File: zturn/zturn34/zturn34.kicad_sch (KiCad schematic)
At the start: 37 parts, among them U1 74AXP4T245, U10 74AXP4T245, U11 74AXP4T245, U12 74AXP4T245, U2 74AXP4T245, U3 74AXP4T245, U4 74AXP4T245, U5 74AXP4T245, U9 74AXP4T245

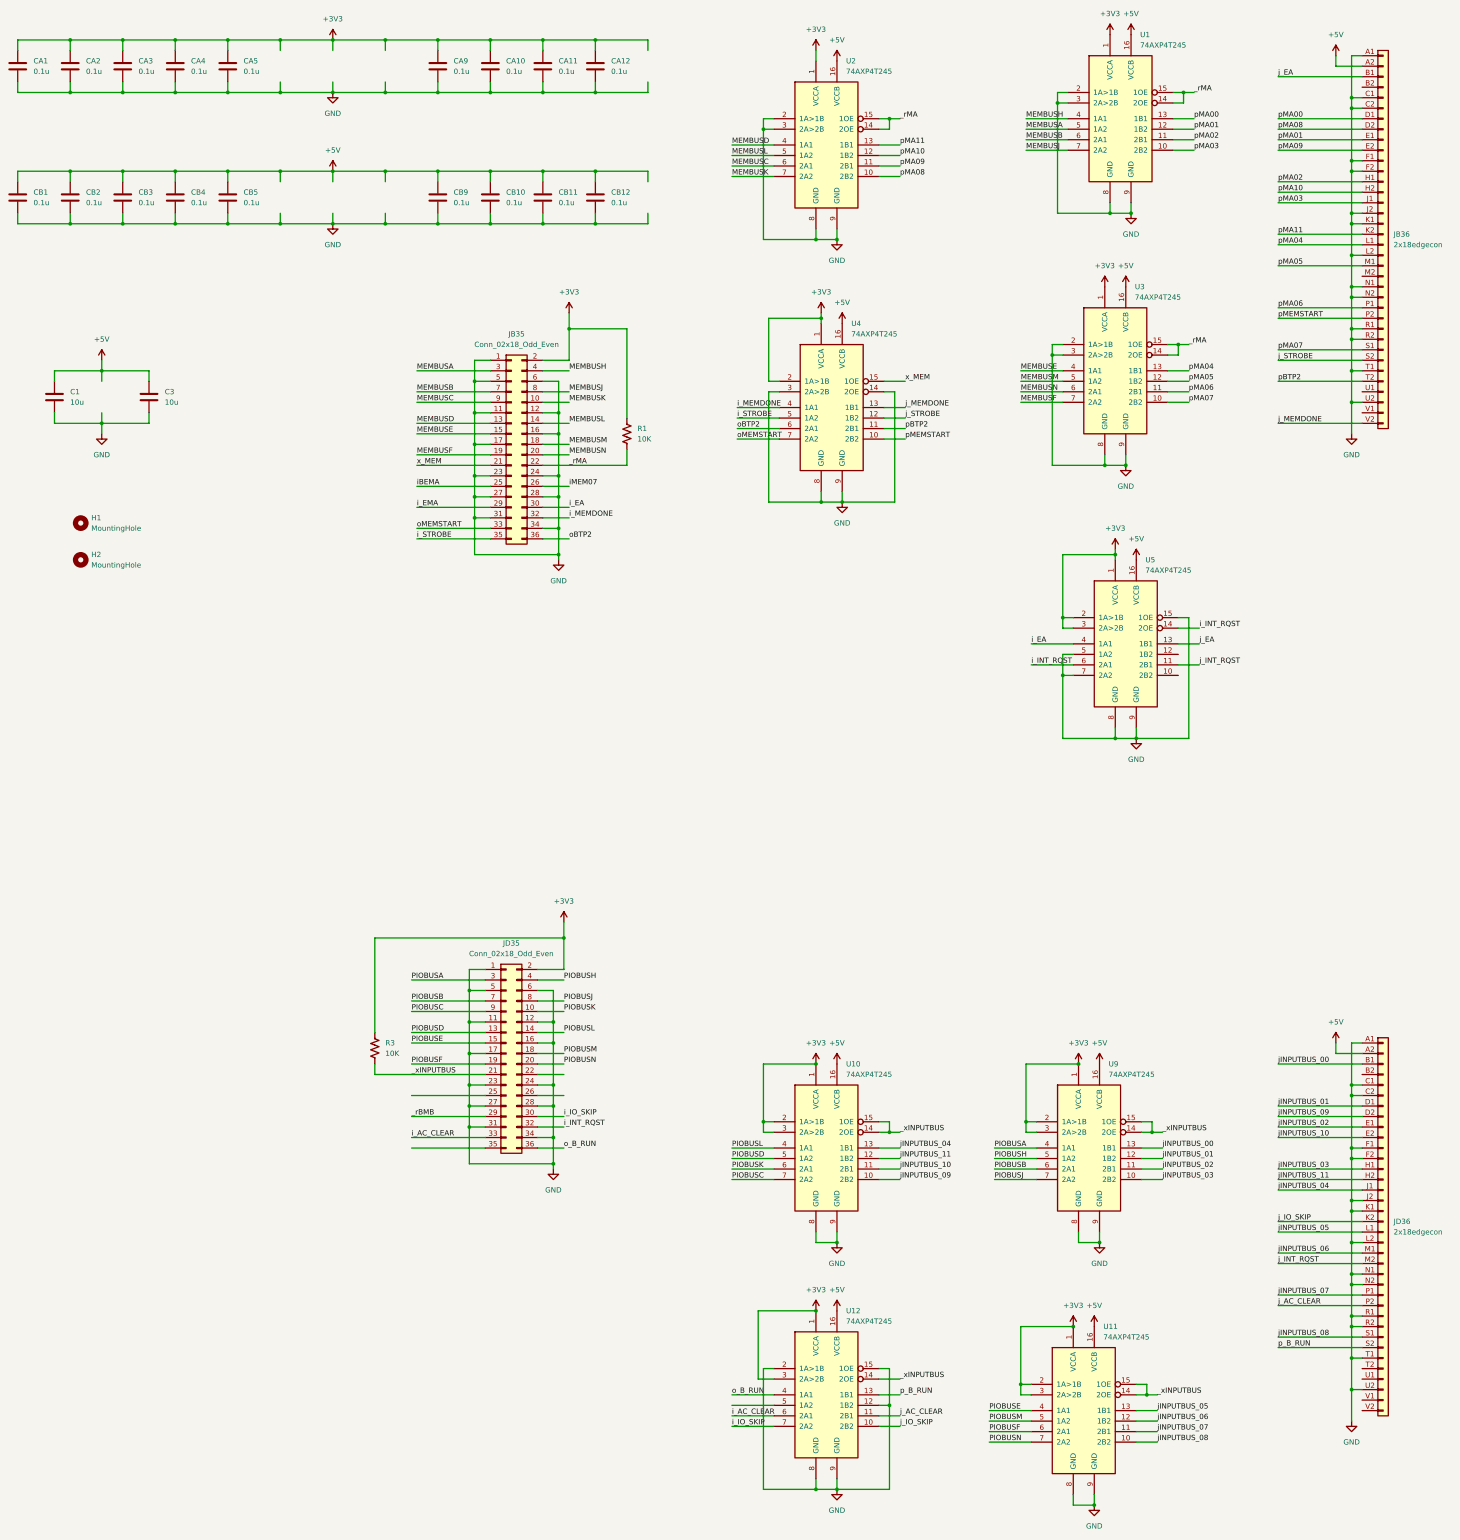
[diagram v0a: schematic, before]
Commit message: update zturn34,35 pcbs - move 10uF caps, add fiducials
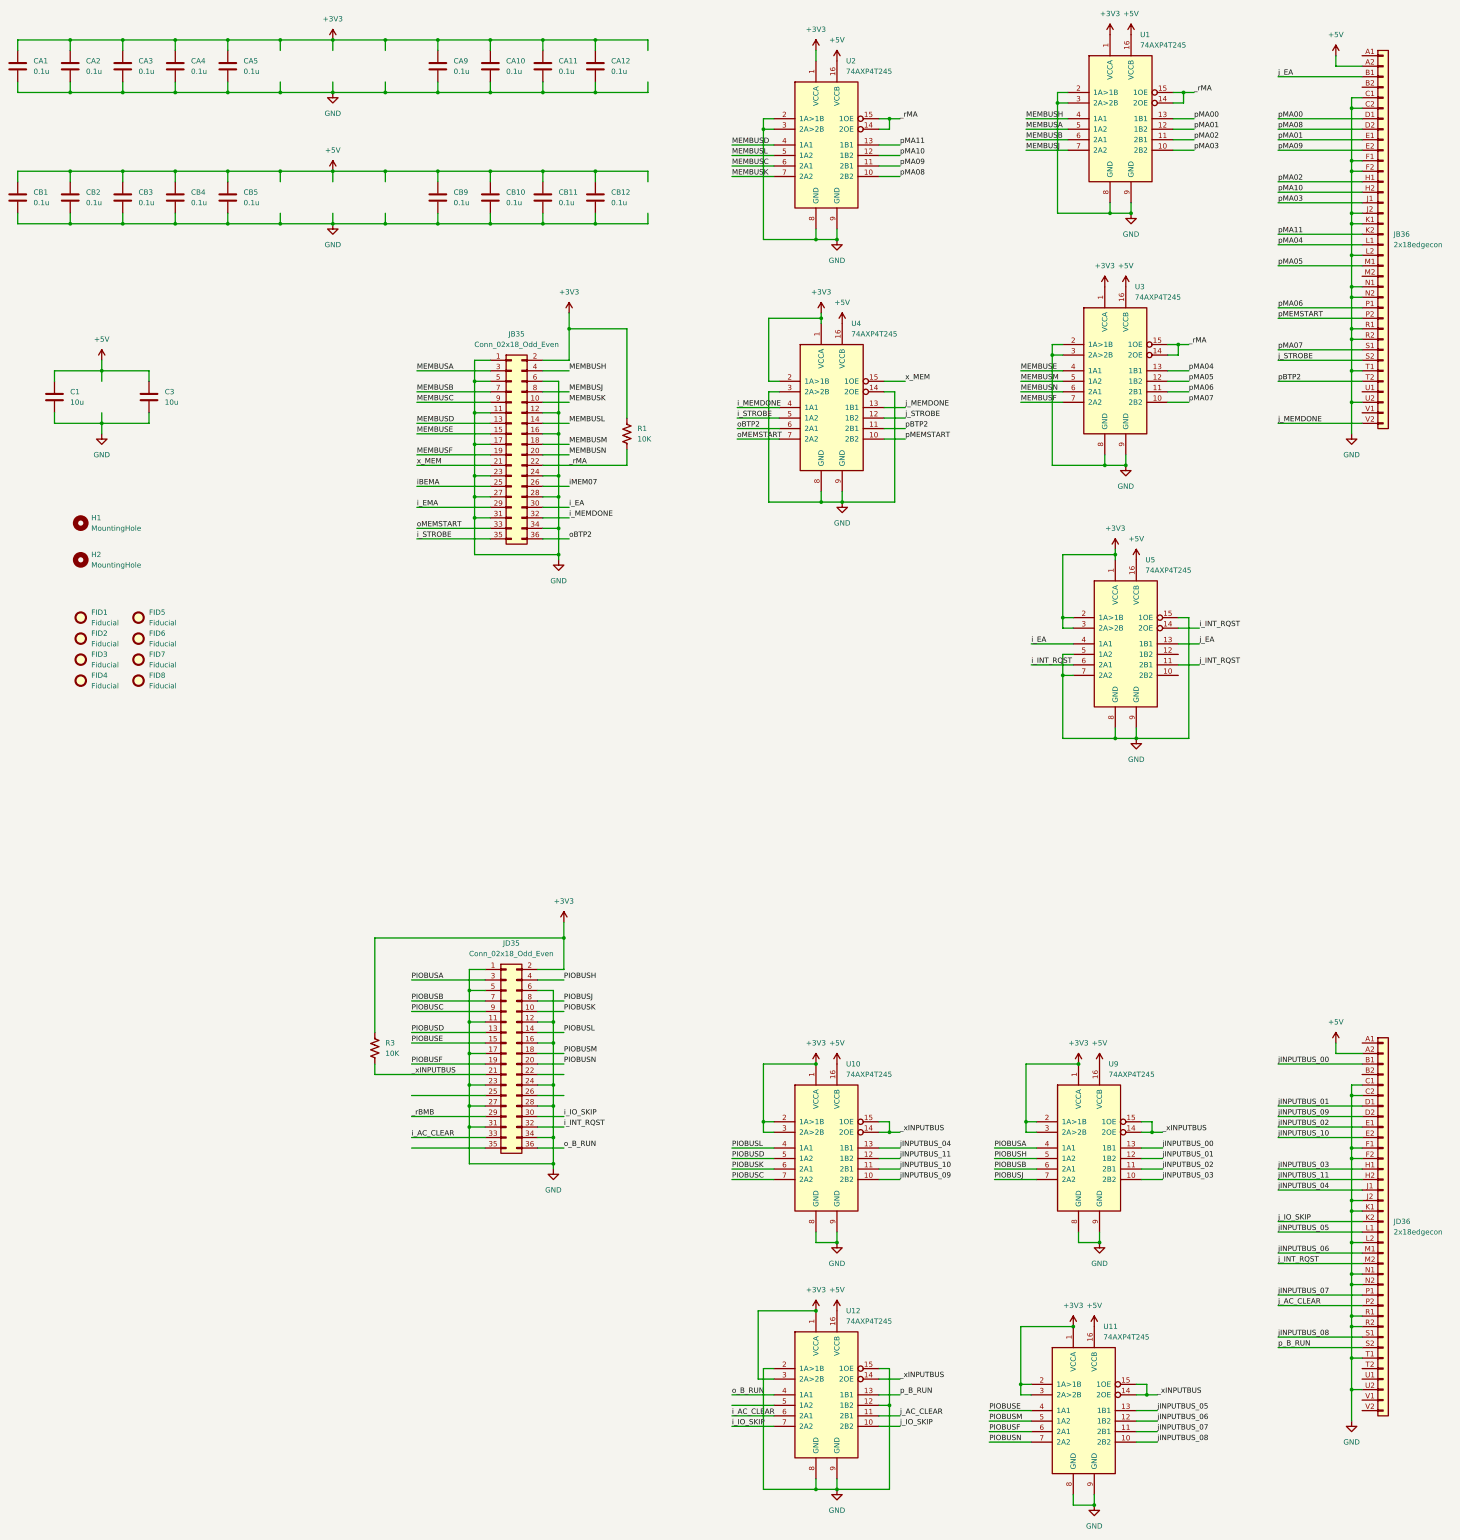
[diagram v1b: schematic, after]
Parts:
- added FID1, FID2, FID3, FID4, FID5, FID6, FID7, FID8: Fiducial, Fiducial:Fiducial_1mm_Mask2mm, symbol Mechanical:Fiducial
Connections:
- net GND: no longer JB36.A1, JD36.A1
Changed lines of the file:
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@@
   (junction (at 364.49 124.46) (diameter 0) (color 0 0 0 0)
   )
-  (junction (at 576.58 33.02) (diameter 0) (color 0 0 0 0)
-  )
   (junction (at 383.54 256.54) (diameter 0) (color 0 0 0 0)
   )
@@
   (junction (at 447.04 326.39) (diameter 0) (color 0 0 0 0)
   )
-  (junction (at 576.58 271.78) (diameter 0) (color 0 0 0 0)
-  )
   (junction (at 521.97 121.92) (diameter 0) (color 0 0 0 0)
   )
@@
     (stroke (width 0) (type default))
   )
-  (wire (pts (xy 576.58 22.86) (xy 579.12 22.86))
-    (stroke (width 0) (type default))
-  )
   (wire (pts (xy 393.7 31.75) (xy 406.4 31.75))
     (stroke (width 0) (type default))
@@
     (stroke (width 0) (type default))
   )
-  (wire (pts (xy 576.58 271.78) (xy 576.58 261.62))
-    (stroke (width 0) (type default))
-  )
   (wire (pts (xy 379.73 254) (xy 386.08 254))
     (stroke (width 0) (type default))
@@
     (stroke (width 0) (type default))
   )
-  (wire (pts (xy 576.58 261.62) (xy 579.12 261.62))
-    (stroke (width 0) (type default))
-  )
   (wire (pts (xy 532.13 99.06) (xy 537.21 99.06))
     (stroke (width 0) (type default))
@@
     (stroke (width 0) (type default))
   )
-  (wire (pts (xy 576.58 33.02) (xy 576.58 22.86))
-    (stroke (width 0) (type default))
-  )
   (wire (pts (xy 534.67 170.18) (xy 539.75 170.18))
     (stroke (width 0) (type default))
@@
     )
   )
+  (symbol (lib_id "Mechanical:Fiducial") (at 283.21 168.91 0) (unit 1)
+    (in_bom yes) (on_board yes) (dnp no) (fields_autoplaced)
+    (property "Reference" "FID7" (at 285.75 167.64 0)
+      (effects (font (size 1.27 1.27)) (justify left))
+    )
+    (property "Value" "Fiducial" (at 285.75 170.18 0)
+      (effects (font (size 1.27 1.27)) (justify left))
+    )
+    (property "Footprint" "Fiducial:Fiducial_1mm_Mask2mm" (at 283.21 168.91 0)
+      (effects (font (size 1.27 1.27)) hide)
+    )
+    (property "Datasheet" "~" (at 283.21 168.91 0)
+      (effects (font (size 1.27 1.27)) hide)
+    )
+    (instances
+      (project "zturn34"
+        (path "/f88ff33f-ea83-4481-9378-71bec9a888d0"
+          (reference "FID7") (unit 1)
+        )
+      )
+    )
+  )
   (symbol (lib_id "power:+5V") (at 572.77 261.62 0) (unit 1)
     (in_bom yes) (on_board yes) (dnp no) (fields_autoplaced)
@@
     )
   )
+  (symbol (lib_id "Mechanical:Fiducial") (at 269.24 158.75 0) (unit 1)
+    (in_bom yes) (on_board yes) (dnp no) (fields_autoplaced)
+    (property "Reference" "FID1" (at 271.78 157.48 0)
+      (effects (font (size 1.27 1.27)) (justify left))
+    )
+    (property "Value" "Fiducial" (at 271.78 160.02 0)
+      (effects (font (size 1.27 1.27)) (justify left))
+    )
+    (property "Footprint" "Fiducial:Fiducial_1mm_Mask2mm" (at 269.24 158.75 0)
+      (effects (font (size 1.27 1.27)) hide)
+    )
+    (property "Datasheet" "~" (at 269.24 158.75 0)
+      (effects (font (size 1.27 1.27)) hide)
+    )
+    (instances
+      (project "zturn34"
+        (path "/f88ff33f-ea83-4481-9378-71bec9a888d0"
+          (reference "FID1") (unit 1)
+        )
+      )
+    )
+  )
   (symbol (lib_name "GND_1") (lib_id "power:GND") (at 330.2 63.5 0) (unit 1)
     (in_bom yes) (on_board yes) (dnp no) (fields_autoplaced)
@@
     )
   )
+  (symbol (lib_id "Mechanical:Fiducial") (at 269.24 168.91 0) (unit 1)
+    (in_bom yes) (on_board yes) (dnp no) (fields_autoplaced)
+    (property "Reference" "FID3" (at 271.78 167.64 0)
+      (effects (font (size 1.27 1.27)) (justify left))
+    )
+    (property "Value" "Fiducial" (at 271.78 170.18 0)
+      (effects (font (size 1.27 1.27)) (justify left))
+    )
+    (property "Footprint" "Fiducial:Fiducial_1mm_Mask2mm" (at 269.24 168.91 0)
+      (effects (font (size 1.27 1.27)) hide)
+    )
+    (property "Datasheet" "~" (at 269.24 168.91 0)
+      (effects (font (size 1.27 1.27)) hide)
+    )
+    (instances
+      (project "zturn34"
+        (path "/f88ff33f-ea83-4481-9378-71bec9a888d0"
+          (reference "FID3") (unit 1)
+        )
+      )
+    )
+  )
   (symbol (lib_id "mylibrary:2x18edgecon") (at 584.2 304.8 0) (unit 1)
     (in_bom yes) (on_board yes) (dnp no) (fields_autoplaced)
@@
     )
   )
+  (symbol (lib_id "Mechanical:Fiducial") (at 269.24 173.99 0) (unit 1)
+    (in_bom yes) (on_board yes) (dnp no) (fields_autoplaced)
+    (property "Reference" "FID4" (at 271.78 172.72 0)
+      (effects (font (size 1.27 1.27)) (justify left))
+    )
+    (property "Value" "Fiducial" (at 271.78 175.26 0)
+      (effects (font (size 1.27 1.27)) (justify left))
+    )
+    (property "Footprint" "Fiducial:Fiducial_1mm_Mask2mm" (at 269.24 173.99 0)
+      (effects (font (size 1.27 1.27)) hide)
+    )
+    (property "Datasheet" "~" (at 269.24 173.99 0)
+      (effects (font (size 1.27 1.27)) hide)
+    )
+    (instances
+      (project "zturn34"
+        (path "/f88ff33f-ea83-4481-9378-71bec9a888d0"
+          (reference "FID4") (unit 1)
+        )
+      )
+    )
+  )
   (symbol (lib_id "power:+5V") (at 572.77 22.86 0) (unit 1)
     (in_bom yes) (on_board yes) (dnp no) (fields_autoplaced)
@@
     )
   )
+  (symbol (lib_id "Mechanical:Fiducial") (at 283.21 158.75 0) (unit 1)
+    (in_bom yes) (on_board yes) (dnp no) (fields_autoplaced)
+    (property "Reference" "FID5" (at 285.75 157.48 0)
+      (effects (font (size 1.27 1.27)) (justify left))
+    )
+    (property "Value" "Fiducial" (at 285.75 160.02 0)
+      (effects (font (size 1.27 1.27)) (justify left))
+    )
+    (property "Footprint" "Fiducial:Fiducial_1mm_Mask2mm" (at 283.21 158.75 0)
+      (effects (font (size 1.27 1.27)) hide)
+    )
+    (property "Datasheet" "~" (at 283.21 158.75 0)
+      (effects (font (size 1.27 1.27)) hide)
+    )
+    (instances
+      (project "zturn34"
+        (path "/f88ff33f-ea83-4481-9378-71bec9a888d0"
+          (reference "FID5") (unit 1)
+        )
+      )
+    )
+  )
   (symbol (lib_id "power:GND") (at 576.58 114.3 0) (unit 1)
     (in_bom yes) (on_board yes) (dnp no) (fields_autoplaced)
@@
     )
   )
+  (symbol (lib_id "Mechanical:Fiducial") (at 283.21 163.83 0) (unit 1)
+    (in_bom yes) (on_board yes) (dnp no) (fields_autoplaced)
+    (property "Reference" "FID6" (at 285.75 162.56 0)
+      (effects (font (size 1.27 1.27)) (justify left))
+    )
+    (property "Value" "Fiducial" (at 285.75 165.1 0)
+      (effects (font (size 1.27 1.27)) (justify left))
+    )
+    (property "Footprint" "Fiducial:Fiducial_1mm_Mask2mm" (at 283.21 163.83 0)
+      (effects (font (size 1.27 1.27)) hide)
+    )
+    (property "Datasheet" "~" (at 283.21 163.83 0)
+      (effects (font (size 1.27 1.27)) hide)
+    )
+    (instances
+      (project "zturn34"
+        (path "/f88ff33f-ea83-4481-9378-71bec9a888d0"
+          (reference "FID6") (unit 1)
+        )
+      )
+    )
+  )
   (symbol (lib_id "power:+3V3") (at 447.04 21.59 0) (unit 1)
     (in_bom yes) (on_board yes) (dnp no) (fields_autoplaced)
@@
     )
   )
+  (symbol (lib_id "Mechanical:Fiducial") (at 269.24 163.83 0) (unit 1)
+    (in_bom yes) (on_board yes) (dnp no) (fields_autoplaced)
+    (property "Reference" "FID2" (at 271.78 162.56 0)
+      (effects (font (size 1.27 1.27)) (justify left))
+    )
+    (property "Value" "Fiducial" (at 271.78 165.1 0)
+      (effects (font (size 1.27 1.27)) (justify left))
+    )
+    (property "Footprint" "Fiducial:Fiducial_1mm_Mask2mm" (at 269.24 163.83 0)
+      (effects (font (size 1.27 1.27)) hide)
+    )
+    (property "Datasheet" "~" (at 269.24 163.83 0)
+      (effects (font (size 1.27 1.27)) hide)
+    )
+    (instances
+      (project "zturn34"
+        (path "/f88ff33f-ea83-4481-9378-71bec9a888d0"
+          (reference "FID2") (unit 1)
+        )
+      )
+    )
+  )
   (symbol (lib_id "power:GND") (at 452.12 369.57 0) (unit 1)
     (in_bom yes) (on_board yes) (dnp no) (fields_autoplaced)
@@
         )
       )
+    )
+  )
+  (symbol (lib_id "Mechanical:Fiducial") (at 283.21 173.99 0) (unit 1)
+    (in_bom yes) (on_board yes) (dnp no) (fields_autoplaced)
+    (property "Reference" "FID8" (at 285.75 172.72 0)
+      (effects (font (size 1.27 1.27)) (justify left))
+    )
+    (property "Value" "Fiducial" (at 285.75 175.26 0)
+      (effects (font (size 1.27 1.27)) (justify left))
+    )
+    (property "Footprint" "Fiducial:Fiducial_1mm_Mask2mm" (at 283.21 173.99 0)
+      (effects (font (size 1.27 1.27)) hide)
+    )
+    (property "Datasheet" "~" (at 283.21 173.99 0)
+      (effects (font (size 1.27 1.27)) hide)
+    )
+    (instances
+      (project "zturn34"
+        (path "/f88ff33f-ea83-4481-9378-71bec9a888d0"
+          (reference "FID8") (unit 1)
+        )
+      )
